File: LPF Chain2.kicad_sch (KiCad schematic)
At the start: 12 parts

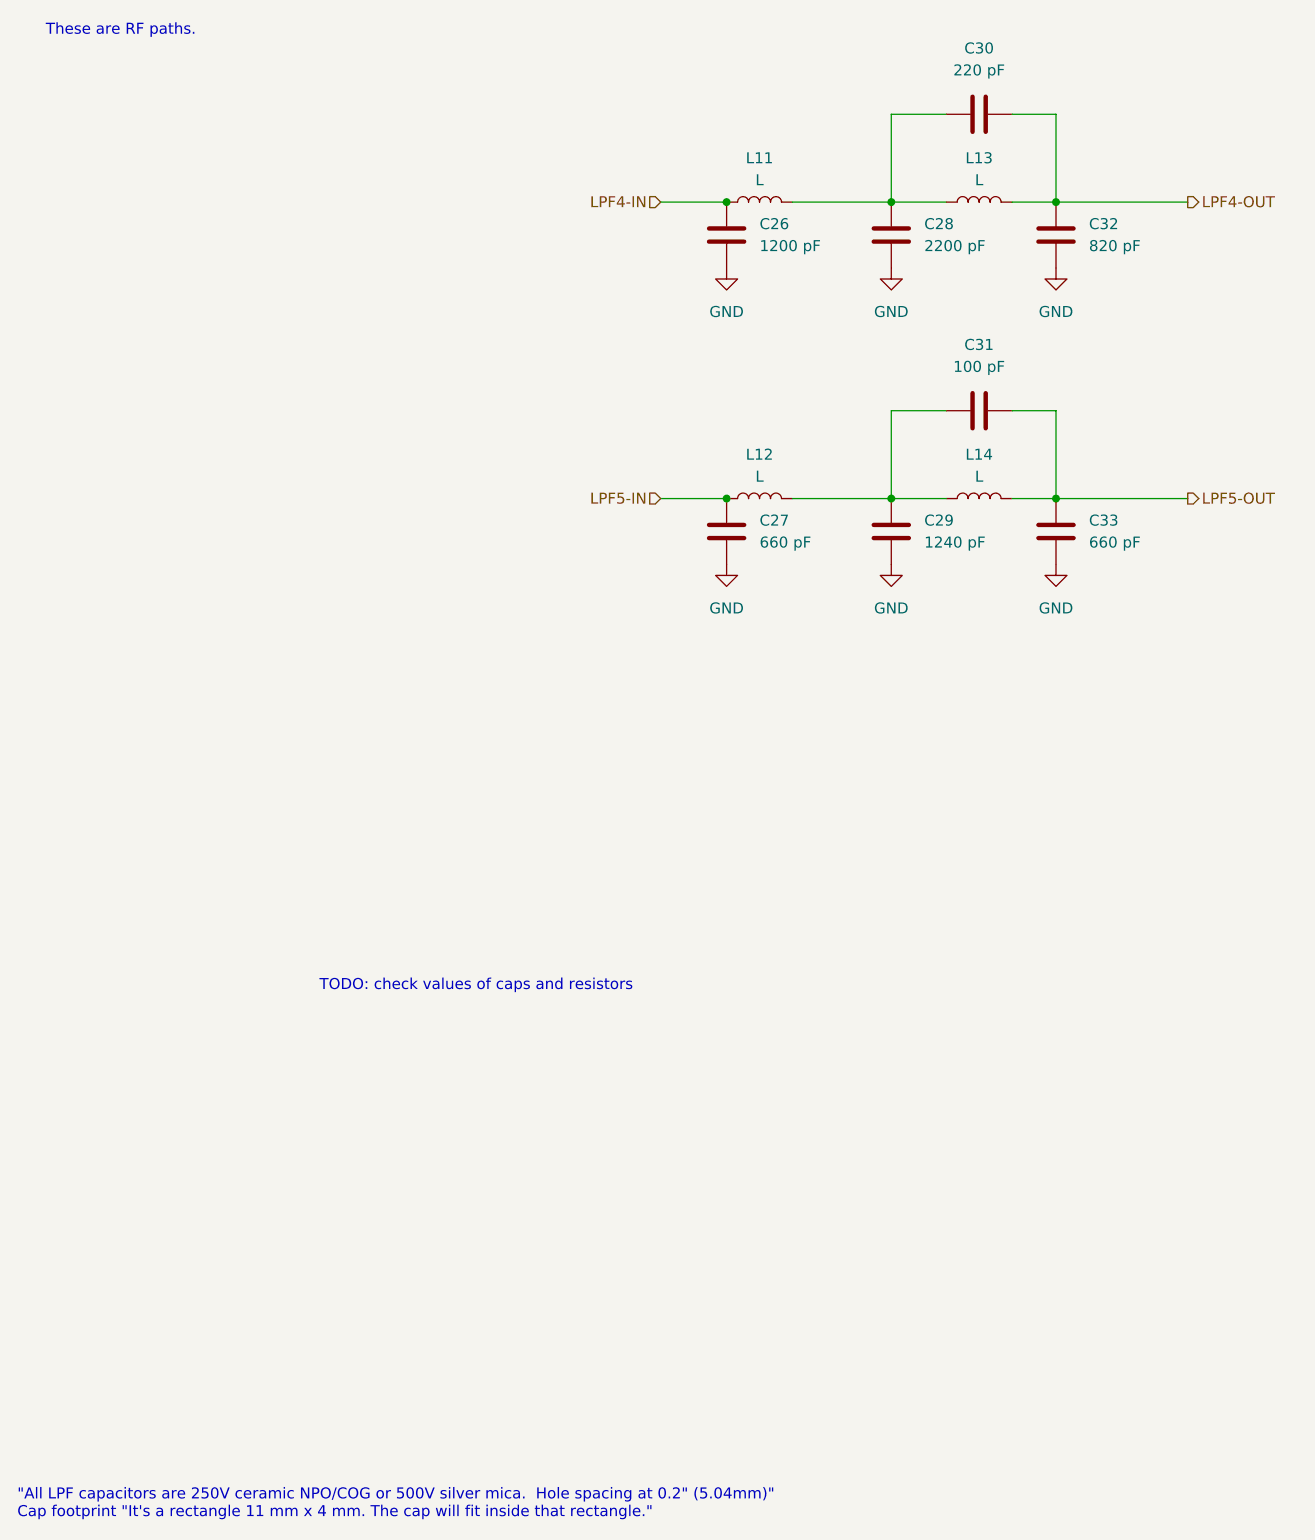
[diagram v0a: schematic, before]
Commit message: v0.9 ERC passes.  All parts have footprints.  Need to renumber pages so things related are closer in printout
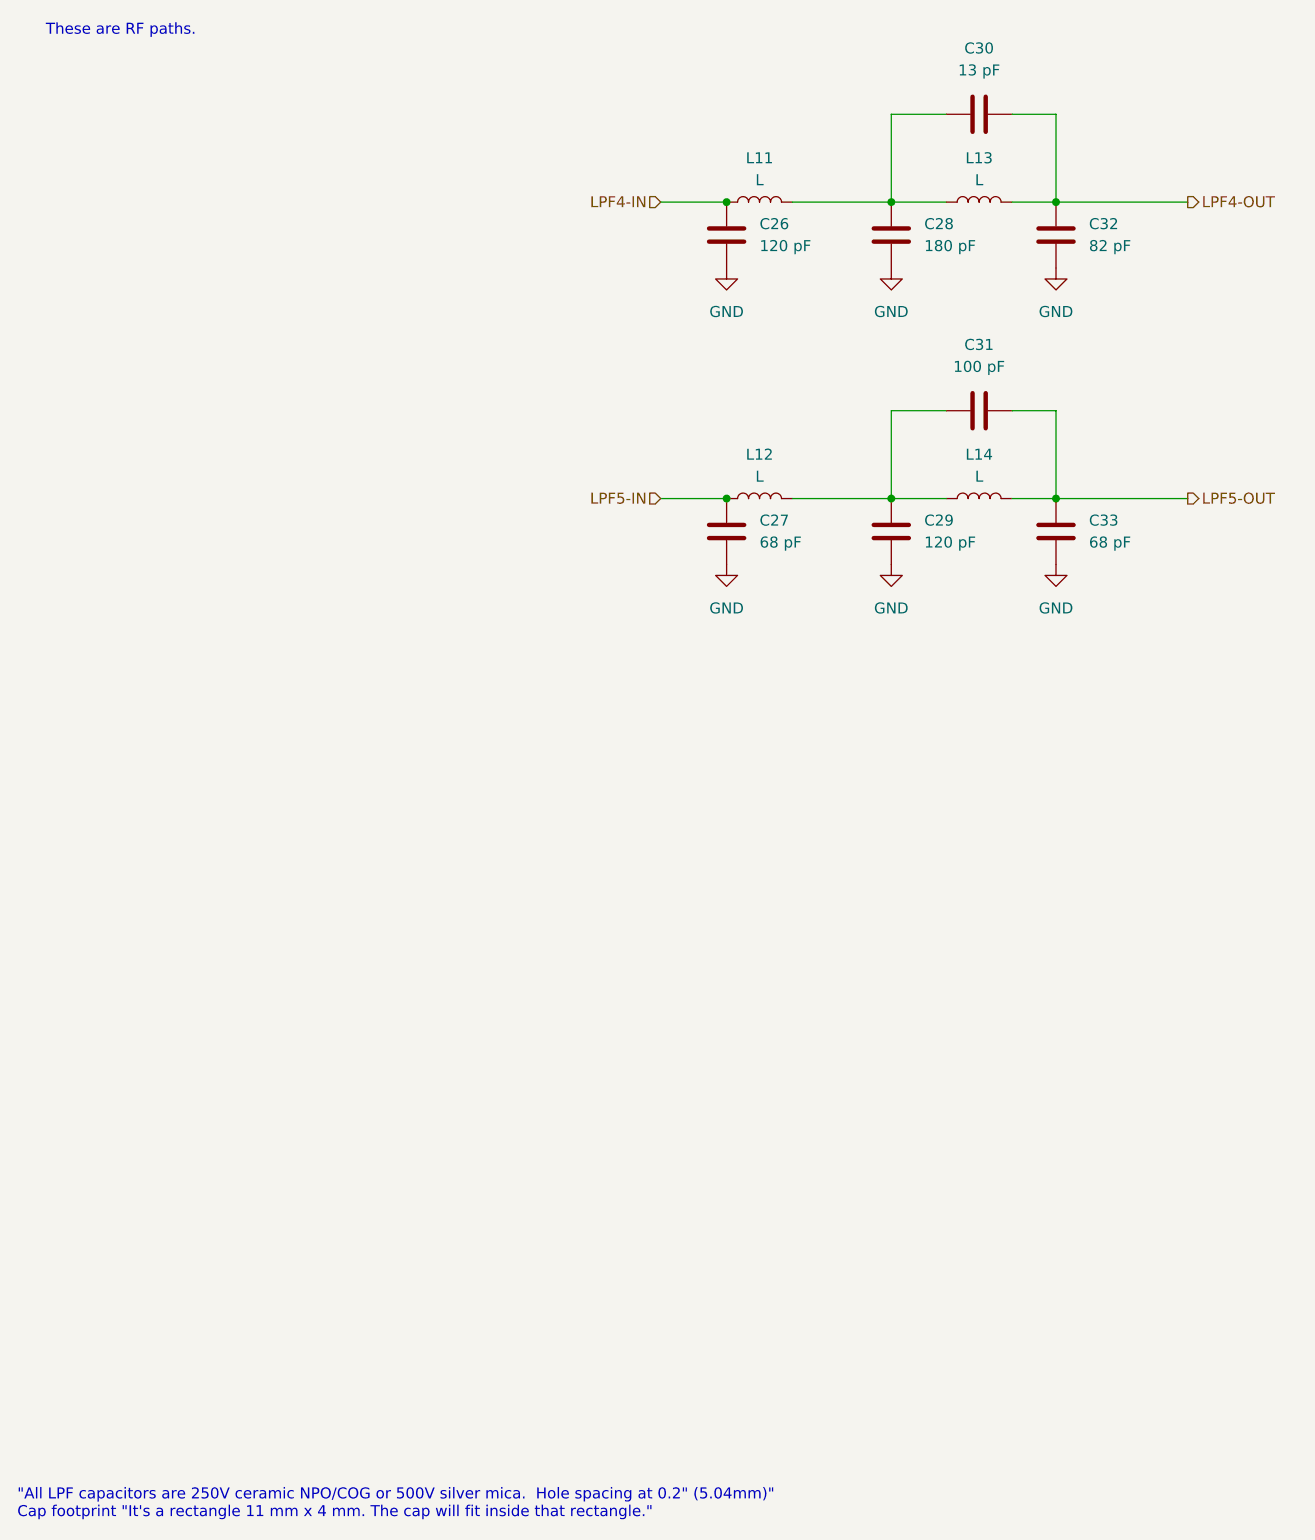
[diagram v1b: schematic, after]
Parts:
- C26: value 1200 pF -> 120 pF
- C27, C33: value 660 pF -> 68 pF
- C28: value 2200 pF -> 180 pF
- C29: value 1240 pF -> 120 pF
- C30: value 220 pF -> 13 pF
- C32: value 820 pF -> 82 pF
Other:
- note removed: "TODO: check values of caps and resistors"
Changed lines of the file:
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@@
 		(title "QMX+ Amp")
 		(date "2024-08-19")
-		(rev "v0.8")
+		(rev "v0.9")
 		(company "WA7GIL")
 	)
@@
 		)
 	)
-	(text "TODO: check values of caps and resistors"
-		(exclude_from_sim no)
-		(at 71.374 132.588 0)
-		(effects
-			(font
-				(size 1.27 1.27)
-			)
-		)
-	)
 	(text "\"All LPF capacitors are 250V ceramic NPO/COG or 500V silver mica.  Hole spacing at 0.2\" (5.04mm)\"\nCap footprint \"It's a rectangle 11 mm x 4 mm. The cap will fit inside that rectangle.\""
 		(exclude_from_sim no)
@@
 			)
 		)
-		(property "Value" "660 pF"
+		(property "Value" "68 pF"
 			(at 142.24 81.2799 0)
 			(effects
@@
 			)
 		)
-		(property "Value" "660 pF"
+		(property "Value" "68 pF"
 			(at 104.14 81.2799 0)
 			(effects
@@
 			)
 		)
-		(property "Value" "220 pF"
+		(property "Value" "13 pF"
 			(at 129.54 26.67 90)
 			(effects
@@
 			)
 		)
-		(property "Value" "1240 pF"
+		(property "Value" "120 pF"
 			(at 123.19 81.2799 0)
 			(effects
@@
 			)
 		)
-		(property "Value" "2200 pF"
+		(property "Value" "180 pF"
 			(at 123.19 46.9899 0)
 			(effects
@@
 			)
 		)
-		(property "Value" "820 pF"
+		(property "Value" "82 pF"
 			(at 142.24 46.9899 0)
 			(effects
@@
 			)
 		)
-		(property "Value" "1200 pF"
+		(property "Value" "120 pF"
 			(at 104.14 46.9899 0)
 			(effects

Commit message: v0.10 after slimming down capacitor width to 3mm so it *barely* fits.
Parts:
- C26, C27, C28, C29, C30, C31, C32, C33: footprint ZZZMyLibrary:C_Disc_D11.0mm_W4.0mm_P5.00mm -> ZZZMyLibrary:C_Disc_D11.0mm_W3.0mm_P5.00mm
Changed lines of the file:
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@@
 			)
 		)
-		(property "Footprint" "ZZZMyLibrary:C_Disc_D11.0mm_W4.0mm_P5.00mm"
+		(property "Footprint" "ZZZMyLibrary:C_Disc_D11.0mm_W3.0mm_P5.00mm"
 			(at 139.3952 83.82 0)
 			(effects
@@
 			)
 		)
-		(property "Footprint" "ZZZMyLibrary:C_Disc_D11.0mm_W4.0mm_P5.00mm"
+		(property "Footprint" "ZZZMyLibrary:C_Disc_D11.0mm_W3.0mm_P5.00mm"
 			(at 133.35 65.0748 0)
 			(effects
@@
 			)
 		)
-		(property "Footprint" "ZZZMyLibrary:C_Disc_D11.0mm_W4.0mm_P5.00mm"
+		(property "Footprint" "ZZZMyLibrary:C_Disc_D11.0mm_W3.0mm_P5.00mm"
 			(at 101.2952 83.82 0)
 			(effects
@@
 			)
 		)
-		(property "Footprint" "ZZZMyLibrary:C_Disc_D11.0mm_W4.0mm_P5.00mm"
+		(property "Footprint" "ZZZMyLibrary:C_Disc_D11.0mm_W3.0mm_P5.00mm"
 			(at 133.35 30.7848 0)
 			(effects
@@
 			)
 		)
-		(property "Footprint" "ZZZMyLibrary:C_Disc_D11.0mm_W4.0mm_P5.00mm"
+		(property "Footprint" "ZZZMyLibrary:C_Disc_D11.0mm_W3.0mm_P5.00mm"
 			(at 120.3452 83.82 0)
 			(effects
@@
 			)
 		)
-		(property "Footprint" "ZZZMyLibrary:C_Disc_D11.0mm_W4.0mm_P5.00mm"
+		(property "Footprint" "ZZZMyLibrary:C_Disc_D11.0mm_W3.0mm_P5.00mm"
 			(at 118.4148 41.91 0)
 			(effects
@@
 			)
 		)
-		(property "Footprint" "ZZZMyLibrary:C_Disc_D11.0mm_W4.0mm_P5.00mm"
+		(property "Footprint" "ZZZMyLibrary:C_Disc_D11.0mm_W3.0mm_P5.00mm"
 			(at 139.3952 49.53 0)
 			(effects
@@
 			)
 		)
-		(property "Footprint" "ZZZMyLibrary:C_Disc_D11.0mm_W4.0mm_P5.00mm"
+		(property "Footprint" "ZZZMyLibrary:C_Disc_D11.0mm_W3.0mm_P5.00mm"
 			(at 101.2952 49.53 0)
 			(effects
